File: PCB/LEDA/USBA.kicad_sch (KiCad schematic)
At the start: 23 parts, among them J1 USB_A, J2 Conn_01x03, T1 T3902_MEMS_Mic, U1 IRM-H638T/TR2, U2 ESP32-S3-MINI-1, U5 MD8942

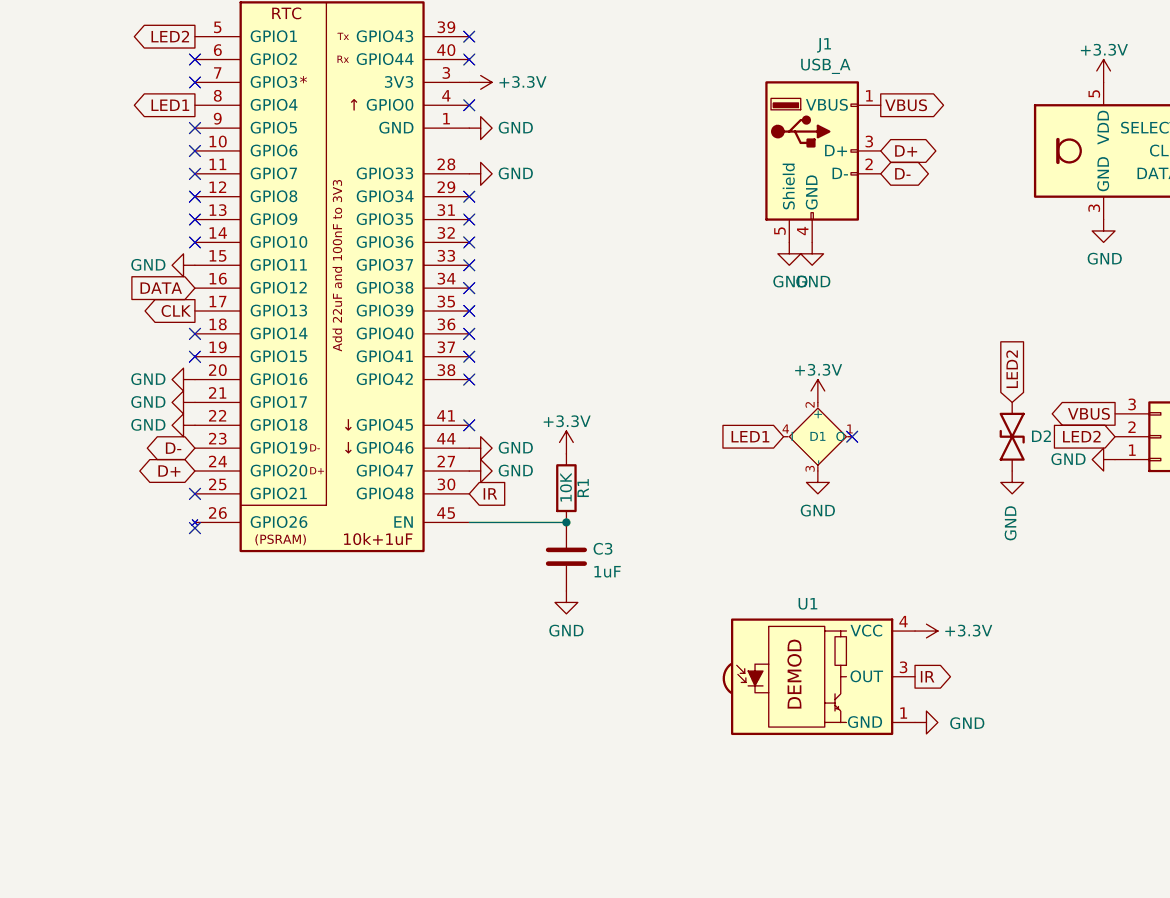
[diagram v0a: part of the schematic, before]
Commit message: Retrack to move USB away from power
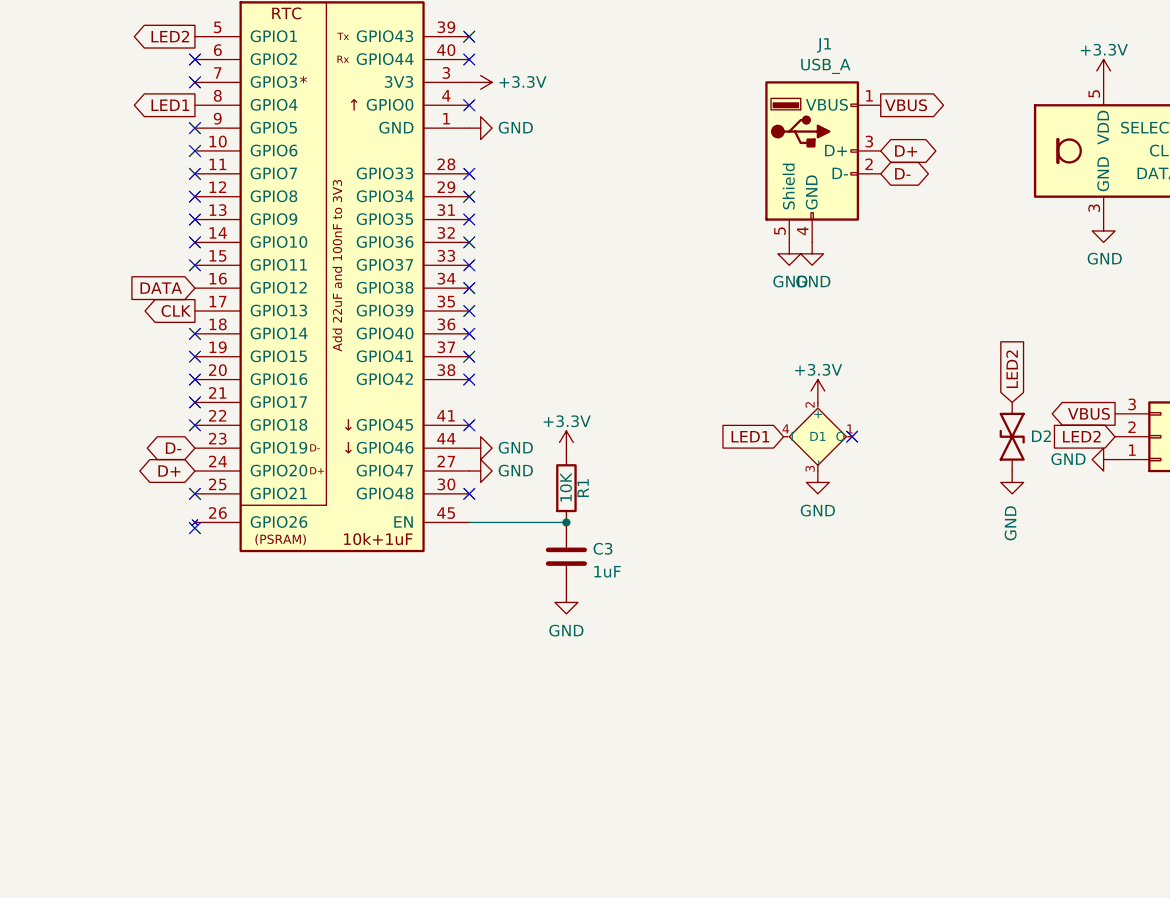
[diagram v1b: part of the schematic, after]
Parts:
- removed U1: IRM-H638T/TR2, RevK:SMD-4P,4x5mm, symbol RevK:IRM-H638T/TR2
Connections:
- net GND: no longer U2.15 (GPIO11), U2.20 (GPIO16), U2.21 (GPIO17), U2.22 (GPIO18), U2.28 (GPIO33)
- net IR: no longer names the net of U2.30 (GPIO48)
- no-connect marks 28 -> 34

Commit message: LEFT
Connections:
- net +3.3V: now also T1.2 (SELECT)
- net GND: no longer T1.2 (SELECT)
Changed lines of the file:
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@@
+	)
+	(symbol
+		(lib_id "power:+3.3V")
+		(at 206.375 62.865 270)
+		(unit 1)
+		(exclude_from_sim no)
+		(in_bom yes)
+		(on_board yes)
+		(dnp no)
+		(fields_autoplaced yes)
+		(property "Reference" "#PWR05"
+			(at 202.565 62.865 0)
+			(effects
+				(font
+					(size 1.27 1.27)
+				)
+				(hide yes)
+			)
+		)
+		(property "Value" "+3.3V"
+			(at 209.55 62.865 90)
+			(effects
+				(font
+					(size 1.27 1.27)
+				)
+				(justify left)
+			)
+		)
+		(property "Footprint" ""
+			(at 206.375 62.865 0)
+			(effects
+				(font
+					(size 1.27 1.27)
+				)
+				(hide yes)
+			)
+		)
+		(property "Datasheet" ""
+			(at 206.375 62.865 0)
+			(effects
+				(font
+					(size 1.27 1.27)
+				)
+				(hide yes)
+			)
+		)
+		(property "Description" "Power symbol creates a global label with name \"+3.3V\""
+			(at 206.375 62.865 0)
+			(effects
+				(font
+					(size 1.27 1.27)
+				)
+				(hide yes)
+			)
+		)
+		(pin "1"
+		)
+		(instances
+			(project "USBA"
+				(path "/2d210a96-f81f-42a9-8bf4-1b43c11086f3"
+					(reference "#PWR05")
+					(unit 1)
+				)
+			)
+		)
 	)
 	(symbol
@@
 					(unit 1)
 				)
-			)
-		)
-	)
-	(symbol
-		(lib_id "power:GND")
-		(at 206.375 62.865 90)
-		(unit 1)
-		(exclude_from_sim no)
-		(in_bom yes)
-		(on_board yes)
-		(dnp no)
-		(property "Reference" "#PWR026"
-			(at 212.725 62.865 0)
-			(effects
-				(font
-					(size 1.27 1.27)
-				)
-				(hide yes)
-			)
-		)
-		(property "Value" "GND"
-			(at 210.7692 62.738 90)
-			(effects
-				(font
-					(size 1.27 1.27)
-				)
-			)
-		)
-		(property "Footprint" ""
-			(at 206.375 62.865 0)
-			(effects
-				(font
-					(size 1.27 1.27)
-				)
-				(hide yes)
-			)
-		)
-		(property "Datasheet" ""
-			(at 206.375 62.865 0)
-			(effects
-				(font
-					(size 1.27 1.27)
-				)
-				(hide yes)
-			)
-		)
-		(property "Description" "Power symbol creates a global label with name \"GND\" , ground"
-			(at 206.375 62.865 0)
-			(effects
-				(font
-					(size 1.27 1.27)
-				)
-				(hide yes)
-			)
-		)
-		(pin "1"
-		)
-		(instances
-			(project "USBA"
-				(path "/2d210a96-f81f-42a9-8bf4-1b43c11086f3"
-					(reference "#PWR026")
-					(unit 1)
-				)

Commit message: New mic
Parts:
- removed T1: T3902_MEMS_Mic, RevK:T3902_MEMS_Mic, symbol RevK:T3902_MEMS_Mic
- added U1: ICS43434_MEMS_Mic, RevK:ICS43434_MEMS_Mic, symbol RevK:ICS43434_MEMS_Mic
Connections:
- net +3.3V: now also U2.18 (GPIO14), U1.5 (VDD)
- net GND: now also U1.2 (LR), U1.3 (GND)
- net SCK: now reaches U2.19 (GPIO15)
- net SCK: now also U1.4 (SCK)
- net CLK renamed SD
- net SD: now also U1.6 (SD)
- net DATA renamed WS
- net WS: now also U1.1 (WS)
- no-connect marks 34 -> 32

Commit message: ADC and tidy SS
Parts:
- added R2: 124K, RevK:R_0402, symbol Device:R
- added R3: 10K, RevK:R_0402, symbol Device:R
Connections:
- net GND: now also R3.2
- net ADC: now reaches U2.9 (GPIO5)
- net ADC: now also R2.2, R3.1
- net VBUS renamed DC
- net DC: now also R2.1
- no-connect marks 32 -> 31

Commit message: Rework
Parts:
- added J3: TC2030-USB-NL-DS, RevK:Tag-Connect_TC2030-IDC-NL_2x03_P1.27mm_Vertical, symbol RevK:TC2030-USB-NL
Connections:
- net D+: now also J3.4 (D+)
- net D-: now also J3.3 (D-)
- net DC: now also J3.1 (VBUS), J3.2 (VBUS)
- net GND: now also J3.5 (GND), J3.6 (GND)
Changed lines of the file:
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@@
+		)
+	)
+	(global_label "D+"
+		(shape bidirectional)
+		(at 241.3 80.645 0)
+		(fields_autoplaced yes)
+		(effects
+			(font
+				(size 1.27 1.27)
+			)
+			(justify left)
+		)
+		(property "Intersheetrefs" "${INTERSHEET_REFS}"
+			(at 247.4259 80.645 0)
+			(effects
+				(font
+					(size 1.27 1.27)
+				)
+				(justify left)
+				(hide yes)
+			)
 		)
 	)
@@
 		)
 	)
+	(global_label "DC"
+		(shape output)
+		(at 241.3 74.295 0)
+		(fields_autoplaced yes)
+		(effects
+			(font
+				(size 1.27 1.27)
+			)
+			(justify left)
+		)
+		(property "Intersheetrefs" "${INTERSHEET_REFS}"
+			(at 246.171 74.295 0)
+			(effects
+				(font
+					(size 1.27 1.27)
+				)
+				(justify left)
+				(hide yes)
+			)
+		)
+	)
 	(global_label "SD"
 		(shape output)
@@
 		(property "Intersheetrefs" "${INTERSHEET_REFS}"
 			(at 206.2869 68.58 0)
+			(effects
+				(font
+					(size 1.27 1.27)
+				)
+				(justify left)
+				(hide yes)
+			)
+		)
+	)
+	(global_label "D-"
+		(shape bidirectional)
+		(at 241.3 78.105 0)
+		(fields_autoplaced yes)
+		(effects
+			(font
+				(size 1.27 1.27)
+			)
+			(justify left)
+		)
+		(property "Intersheetrefs" "${INTERSHEET_REFS}"
+			(at 247.4259 78.105 0)
 			(effects
 				(font
@@
 	)
 	(symbol
+		(lib_id "RevK:TC2030-USB-NL")
+		(at 233.68 79.375 0)
+		(unit 1)
+		(exclude_from_sim no)
+		(in_bom no)
+		(on_board yes)
+		(dnp no)
+		(fields_autoplaced yes)
+		(property "Reference" "J3"
+			(at 233.68 67.6105 0)
+			(effects
+				(font
+					(size 1.27 1.27)
+				)
+			)
+		)
+		(property "Value" "TC2030-USB-NL-DS"
+			(at 233.68 70.0348 0)
+			(effects
+				(font
+					(size 1.27 1.27)
+				)
+			)
+		)
+		(property "Footprint" "RevK:Tag-Connect_TC2030-IDC-NL_2x03_P1.27mm_Vertical"
+			(at 233.426 88.519 0)
+			(effects
+				(font
+					(size 1.27 1.27)
+				)
+				(hide yes)
+			)
+		)
+		(property "Datasheet" " ~"
+			(at 237.49 80.645 0)
+			(effects
+				(font
+					(size 1.27 1.27)
+				)
+				(hide yes)
+			)
+		)
+		(property "Description" "TC2030-USB-NL"
+			(at 233.68 66.675 0)
+			(effects
+				(font
+					(size 1.27 1.27)
+				)
+				(hide yes)
+			)
+		)
+		(pin "1"
+		)
+		(pin "2"
+		)
+		(pin "3"
+		)
+		(pin "4"
+		)
+		(pin "5"
+		)
+		(pin "6"
+		)
+		(instances
+			(project "USBA"
+				(path "/2d210a96-f81f-42a9-8bf4-1b43c11086f3"
+					(reference "J3")
+					(unit 1)
+				)
+			)
+		)
+	)
+	(symbol
 		(lib_id "power:+3.3V")
 		(at 222.25 45.72 90)
@@
 					(unit 1)
 				)
+			)
+		)
+	)
+	(symbol
+		(lib_id "power:GND")
+		(at 241.3 84.455 90)
+		(unit 1)
+		(exclude_from_sim no)
+		(in_bom yes)
+		(on_board yes)
+		(dnp no)
+		(fields_autoplaced yes)
+		(property "Reference" "#PWR015"
+			(at 247.65 84.455 0)
+			(effects
+				(font
+					(size 1.27 1.27)
+				)
+				(hide yes)
+			)
+		)
+		(property "Value" "GND"
+			(at 244.475 84.455 90)
+			(effects
+				(font
+					(size 1.27 1.27)
+				)
+				(justify right)
+			)
+		)
+		(property "Footprint" ""
+			(at 241.3 84.455 0)
+			(effects
+				(font
+					(size 1.27 1.27)
+				)
+				(hide yes)
+			)
+		)
+		(property "Datasheet" ""
+			(at 241.3 84.455 0)
+			(effects
+				(font
+					(size 1.27 1.27)
+				)
+				(hide yes)
+			)
+		)
+		(property "Description" "Power symbol creates a global label with name \"GND\" , ground"
+			(at 241.3 84.455 0)
+			(effects
+				(font
+					(size 1.27 1.27)
+				)
+				(hide yes)
+			)
+		)
+		(pin "1"
+		)
+		(instances
+			(project "USBA"
+				(path "/2d210a96-f81f-42a9-8bf4-1b43c11086f3"
+					(reference "#PWR015")
+					(unit 1)
+				)
